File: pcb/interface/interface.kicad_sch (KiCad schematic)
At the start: 24 parts, among them J1 Conn_ARM_JTAG_SWD_10, J4 Conn_01x05_Pin, J5 Conn_01x05_Pin, U1 MT6701CT, U2 AP2204K-5.0

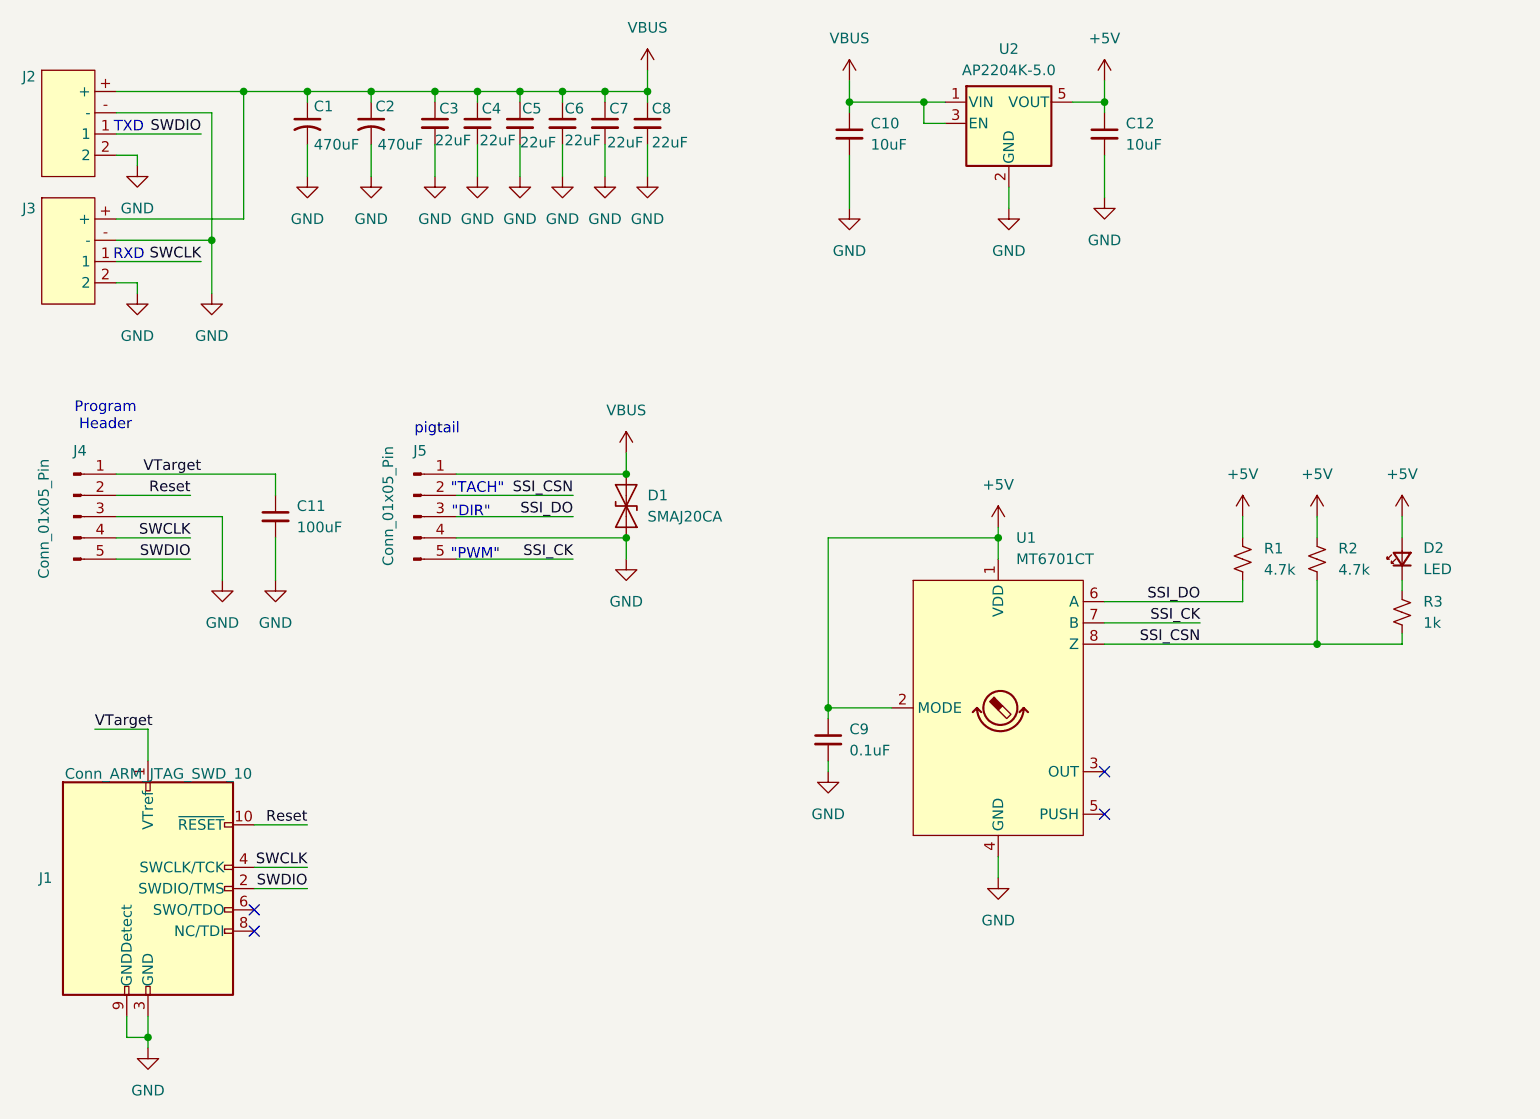
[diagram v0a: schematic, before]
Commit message: fix reversed connector
and add a TVS diode
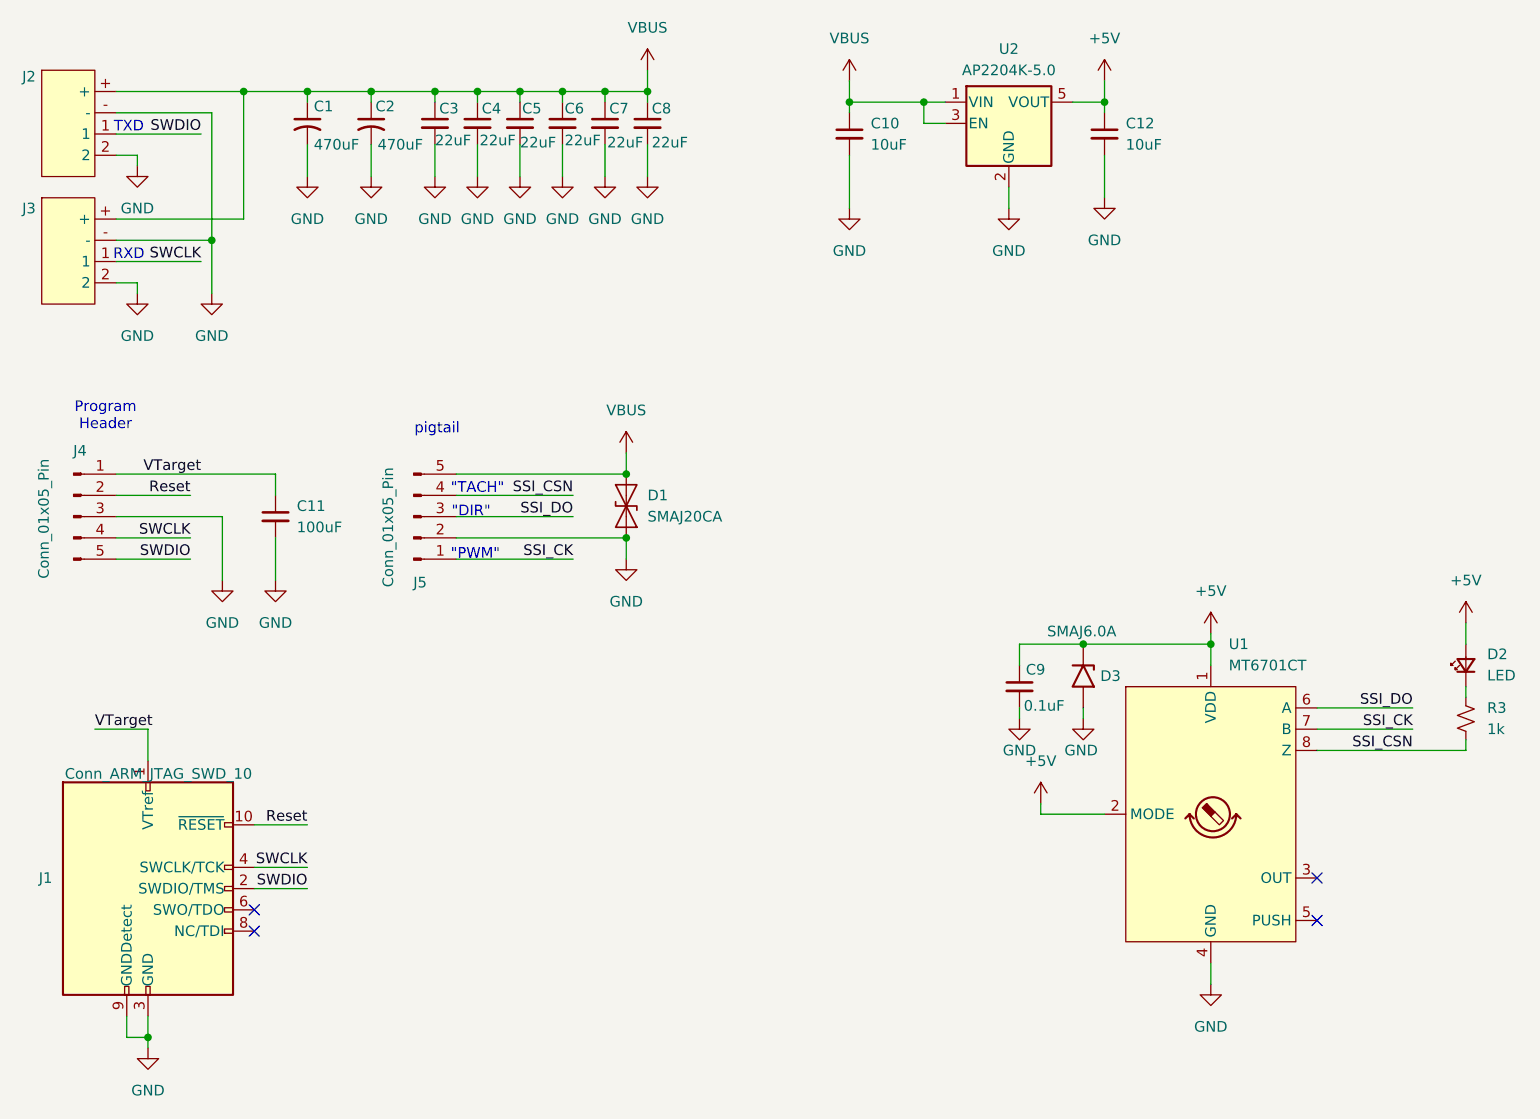
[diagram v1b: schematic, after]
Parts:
- removed R1, R2: 4.7k, Resistor_SMD:R_0603_1608Metric, symbol Device:R_Small_US
- added D3: SMAJ6.0A, Diode_SMD:D_SMA, symbol Diode:SMAJ6.0A
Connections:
- net +5V: now also D3.1 (A1)
- net GND: now also J5.2 (Pin_2), D3.2 (A2); no longer J5.4 (Pin_4)
- net SSI_CK: now also J5.1 (Pin_1); no longer J5.5 (Pin_5)
- net SSI_CSN: now also J5.4 (Pin_4); no longer J5.2 (Pin_2)
- net VBUS: now also J5.5 (Pin_5); no longer J5.1 (Pin_1)
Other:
- moved on the sheet: C9, D2, R3, U1

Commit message: as-ordered V2 interface boards
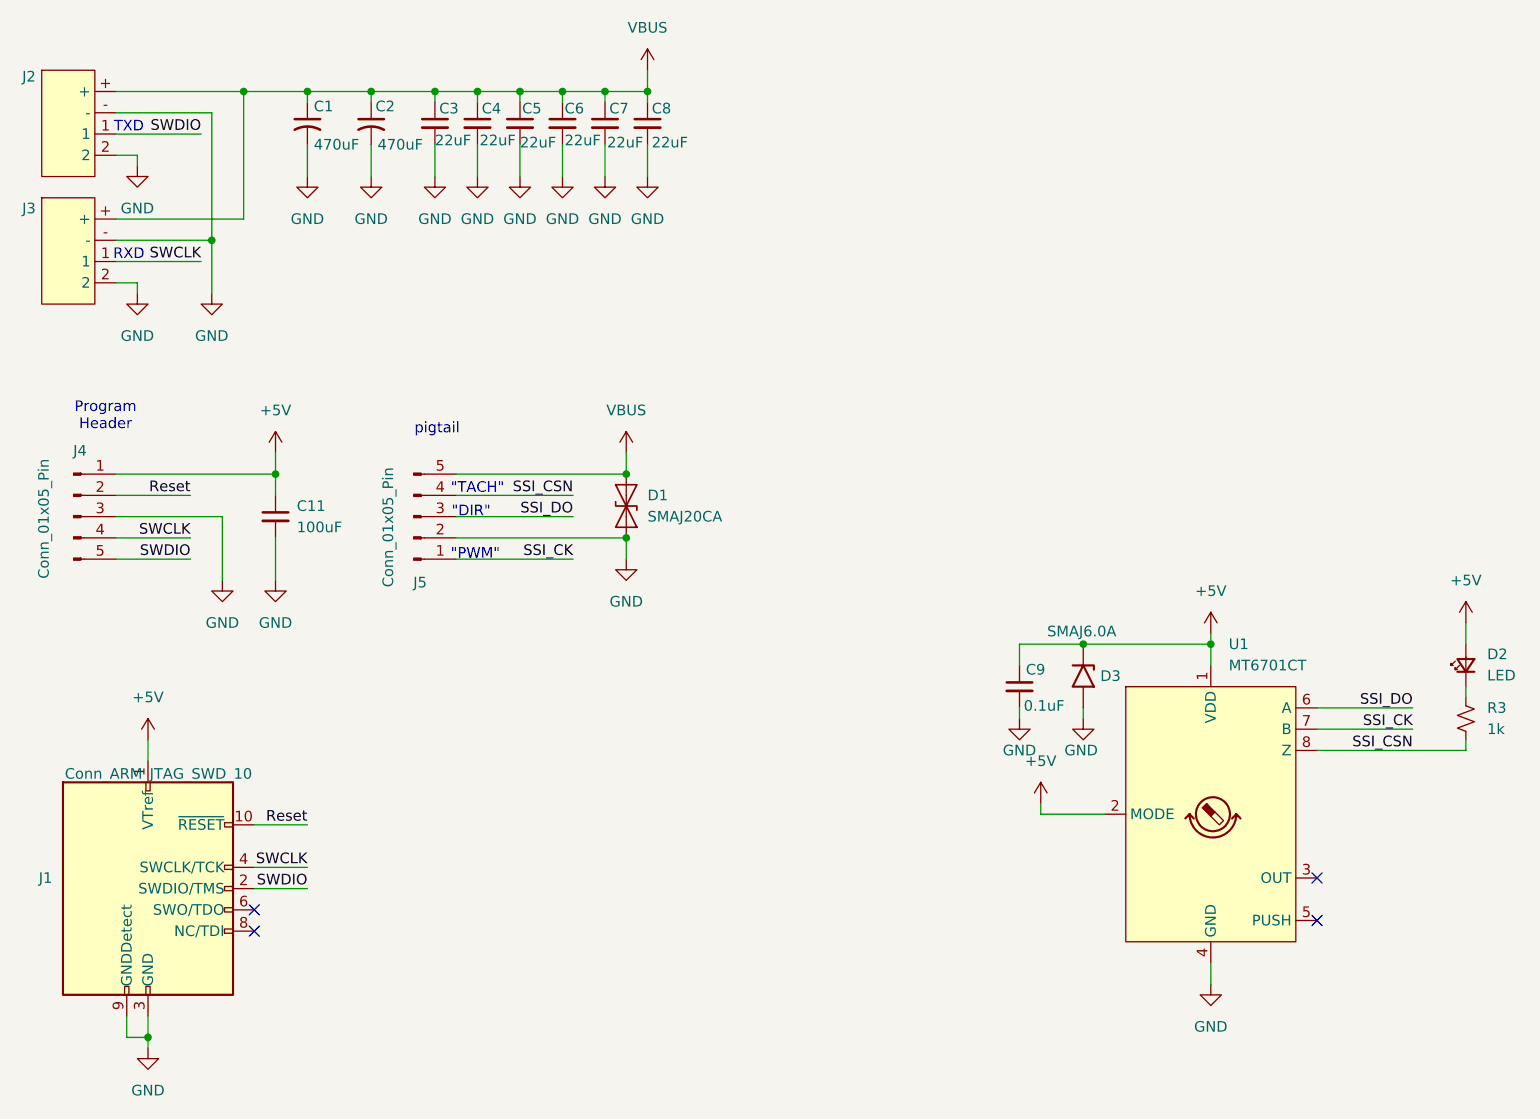
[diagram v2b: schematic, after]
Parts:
- removed C10: 10uF, Capacitor_SMD:C_0805_2012Metric, symbol Device:C_Small
- removed C12: 10uF, Capacitor_SMD:C_0603_1608Metric, symbol Device:C_Small
- removed U2: AP2204K-5.0, Package_TO_SOT_SMD:SOT-23-5, symbol Regulator_Linear:AP2204K-5.0
- J2, J3: value ~ -> (none)
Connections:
- net VTarget is gone; now on net +5V: C11.1, J1.1 (VTref), J4.1 (Pin_1)
